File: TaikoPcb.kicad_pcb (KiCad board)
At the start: 2 copper layers, 65.5 x 54.5 mm, 18 parts, among them J1 Screw_Terminal_01x04, J2 Screw_Terminal_01x04, J3 Screw_Terminal_01x04, U1 ESP32-S3-Supermini, U2 DB107-G, U3 DB107-G, U4 DB107-G, U5 DB107-G

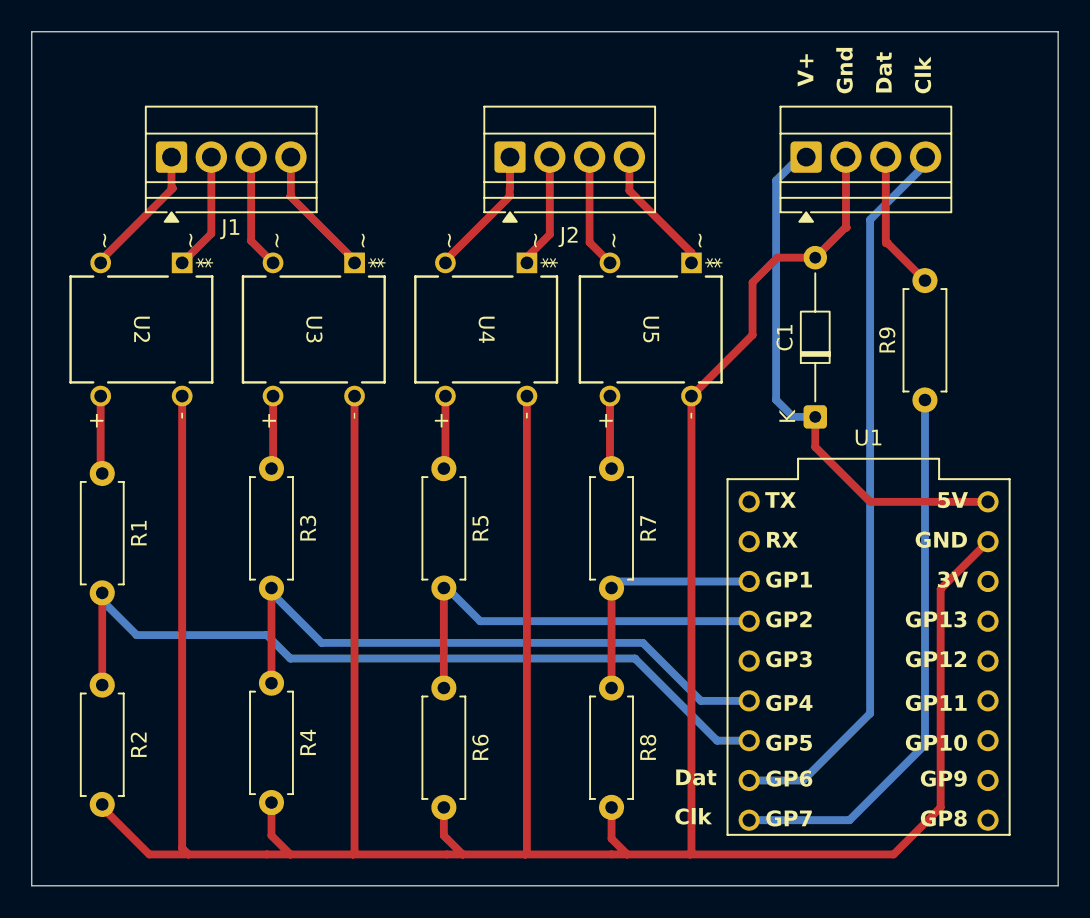
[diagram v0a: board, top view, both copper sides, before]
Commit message: Adjust so that usbc plug can fit
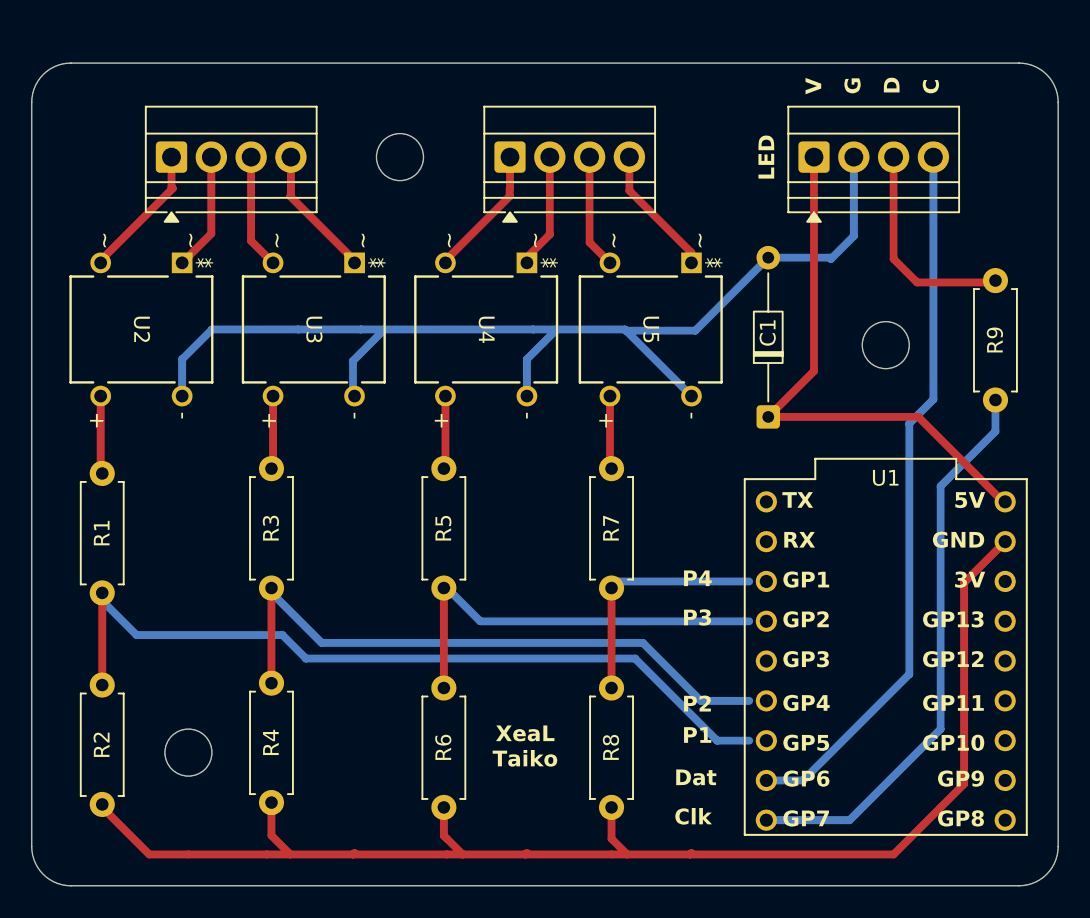
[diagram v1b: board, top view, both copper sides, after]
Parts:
- added ?: , , F.Cu at (166.0, 51.0)
- added REF**: MountingHole_3mm, MountingHole:MountingHole_3mm, F.Cu at (121.5, 77.0)
- added REF**: MountingHole_3mm, MountingHole:MountingHole_3mm, F.Cu at (135.0, 39.0)
- moved R9 4.50 mm to (173.0, 54.5)
- moved C1 3.00 mm to (158.5, 55.6)
- moved U1 1.10 mm to (166.0, 70.9)
- moved J3 0.50 mm to (161.4, 39.0)
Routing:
- net GND: track 223.6 -> 155.7 mm
- net Net-(J3-Pin_3): track 9.04 -> 13.7 mm
- net Net-(J3-Pin_1): track 34.1 -> 35.2 mm
- net Net-(J3-Pin_4): track 46.5 -> 45.6 mm
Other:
- board size 65.5 x 54.5 mm -> 65.5 x 52.5 mm
- board text added: "C"
- board text added: "D"
- board text added: "ESP32 S3 SuperMini"
- board text added: "G"
- board text added: "JLCJLCJLCJLC"
- board text added: "LED"
- board text added: "P1"
- board text added: "P2"
- board text added: "P3"
- board text added: "P4"
- board text added: "V"
- board text added: "XeaL Taiko"
- board text removed: "Gnd"
- board text removed: "V+"

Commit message: More adjustments
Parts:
- removed ?: , 
- added REF**: MountingHole_3mm, MountingHole:MountingHole_3mm, F.Cu at (165.5, 51.0)
- moved REF** 2.50 mm to (121.5, 79.5)
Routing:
- net GND: track 155.7 -> 176.5 mm
- net Net-(U1-GP5): track 51.6 -> 54.9 mm
- net Net-(U1-GP2): track 26.5 -> 29.0 mm
- net Net-(U1-GP1): track 15.3 -> 17.0 mm
- net Net-(U1-GP4): track 39.8 -> 41.4 mm
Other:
- board size 65.5 x 52.5 mm -> 65.5 x 51.5 mm
